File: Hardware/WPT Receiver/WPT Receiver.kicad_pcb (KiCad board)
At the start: 2 copper layers, 100 x 100 mm, 157 parts, among them J1 0.1" Header, J2 Tag-connect-NL, J3 0.1" Header, J4 0.1" Header, SW1 PTS647, SW2 PTS647, SW3 PTS647, U1 STM32G031C6U6, U10 74HC595, U2 INA180A3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

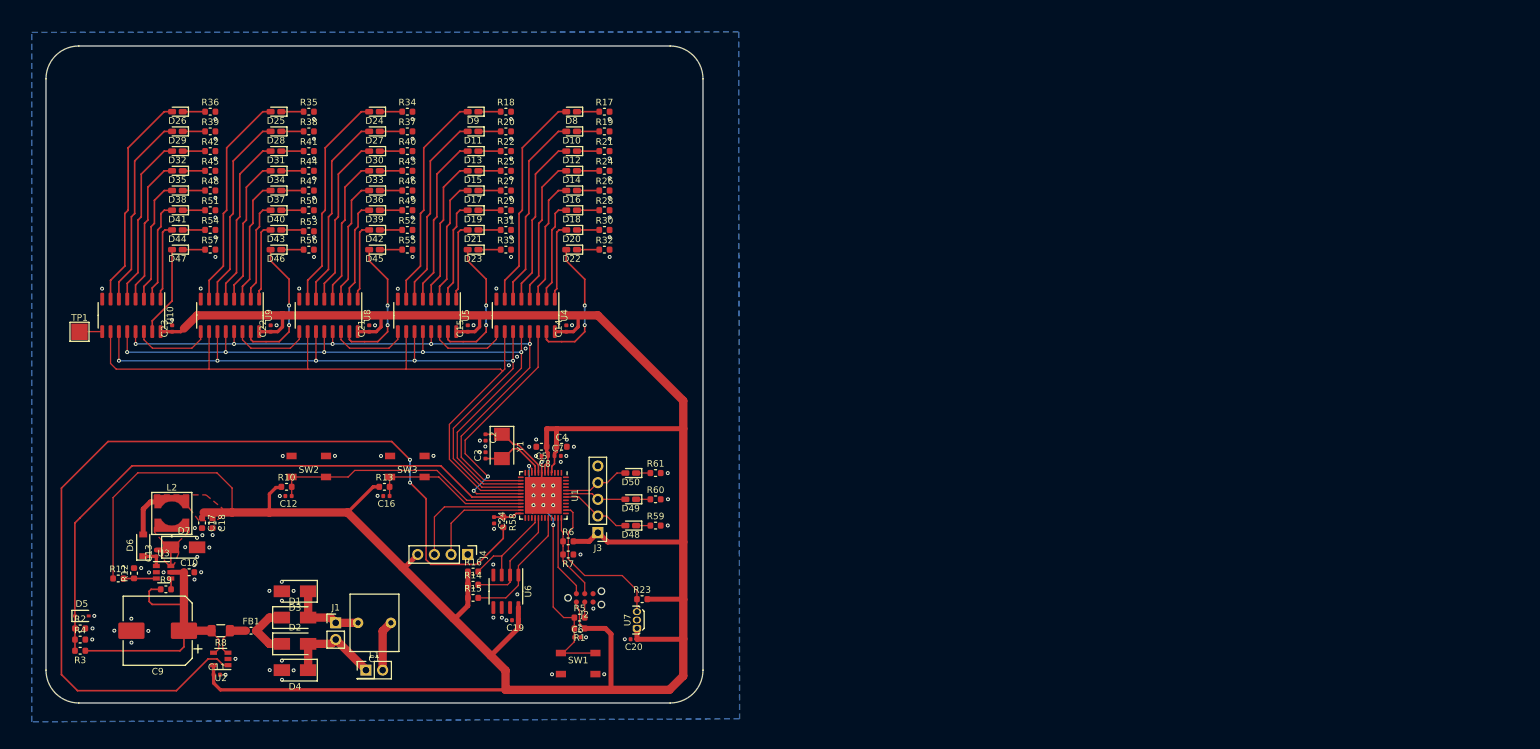
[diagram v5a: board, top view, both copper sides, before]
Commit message: Added tons of ground vias for stiching and to better connect islands. Added logo library and added to board
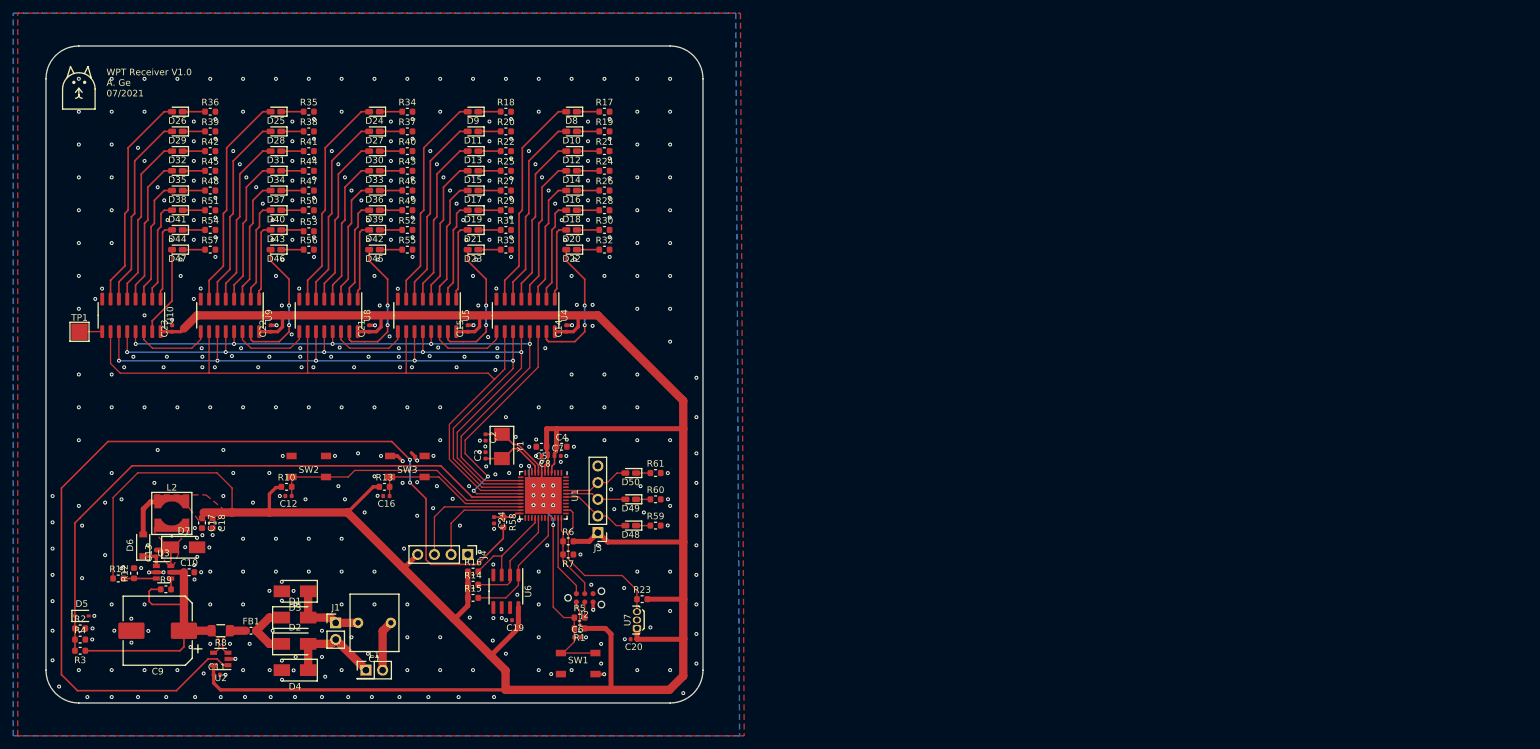
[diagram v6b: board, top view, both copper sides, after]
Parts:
- added REF**: ANDREW_CAT, LOGOS:ANDREW_CAT, F.Cu at (55.0, 59.6)
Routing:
- net GND: track 6.11 -> 19.7 mm, vias 125 -> 466
- net /SRCLR: track 117.9 -> 119.1 mm
- added copper zone on F.Cu, net GND
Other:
- board text added: "WPT Receiver V1.0 A. Ge 07/2021"

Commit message: Added silkscreen labels to headers, positioned all designators. First draft complete
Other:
- board text added: "3V3"
- board text added: "GND"
- board text added: "LD1"
- board text added: "LD2"
- board text added: "LD3"
- board text added: "RST"
- board text added: "RX"
- board text added: "TX"
- board text added: "UB1"
- board text added: "UB2"
